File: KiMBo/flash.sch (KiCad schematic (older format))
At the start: 31 parts, among them IC1 24LC32AT-I/OT, U2 OSD3358, U6 74LVC1G06, U7 EMMC**G-S100

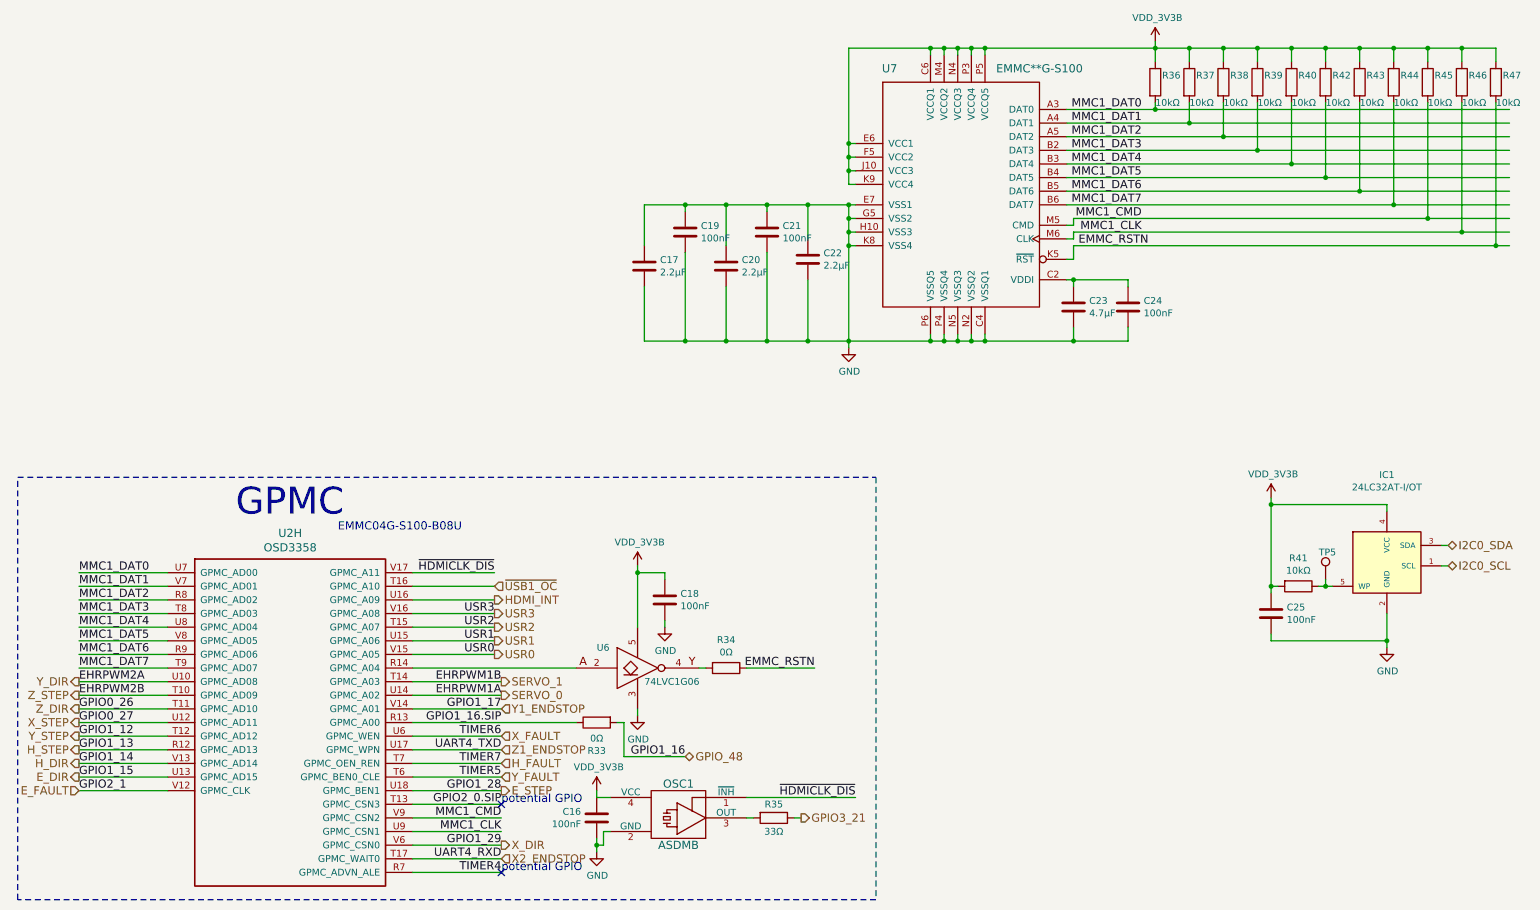
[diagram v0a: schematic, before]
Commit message: Add equivalent annotations document, associate more footprints
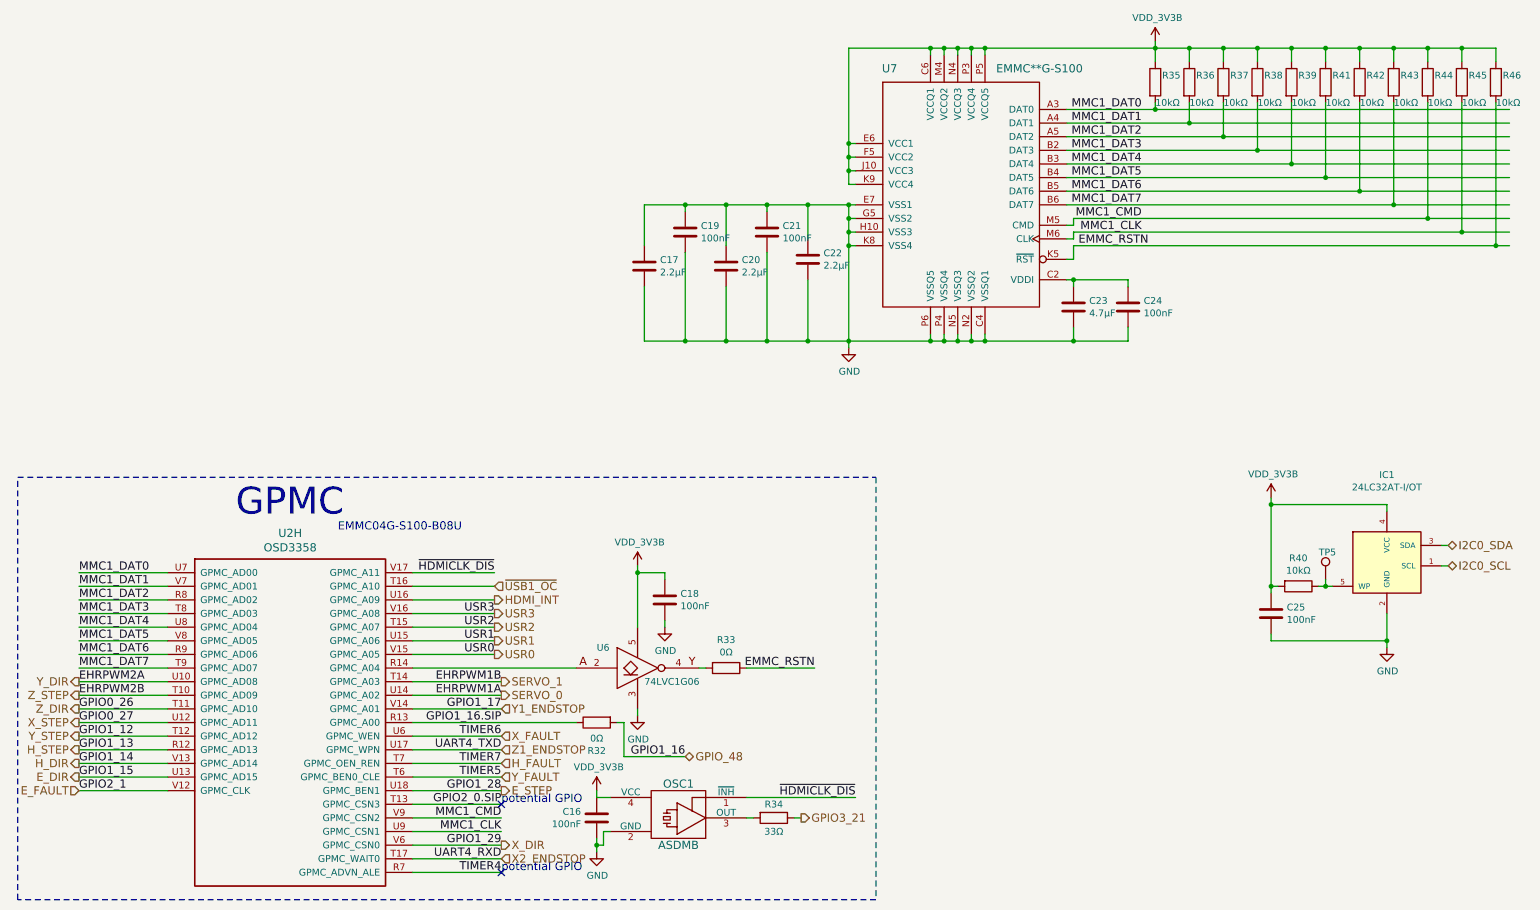
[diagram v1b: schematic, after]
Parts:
- C16, C18, C19, C21, C24, C25: footprint (none) -> Capacitors_SMD:C_0402
- C17, C20, C22, C23: footprint (none) -> Capacitors_SMD:C_0805
- R32: renamed from R33; footprint (none) -> Resistors_SMD:R_0402
- R33: renamed from R34; footprint (none) -> Resistors_SMD:R_0402
- R35: renamed from R36; footprint (none) -> Resistors_SMD:R_0402
- R36: renamed from R37; footprint (none) -> Resistors_SMD:R_0402
- R37: renamed from R38; footprint (none) -> Resistors_SMD:R_0402
- R38: renamed from R39; footprint (none) -> Resistors_SMD:R_0402
- R39: renamed from R40; footprint (none) -> Resistors_SMD:R_0402
- R40: renamed from R41; footprint (none) -> Resistors_SMD:R_0402
- R41: renamed from R42; footprint (none) -> Resistors_SMD:R_0402
- R42: renamed from R43; footprint (none) -> Resistors_SMD:R_0402
- R43: renamed from R44; footprint (none) -> Resistors_SMD:R_0402
- R44: renamed from R45; footprint (none) -> Resistors_SMD:R_0402
- R45: renamed from R46; footprint (none) -> Resistors_SMD:R_0402
- R46: renamed from R47; footprint (none) -> Resistors_SMD:R_0402
- renumbered R35 to R34
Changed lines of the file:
@@
 $EndDescr
 $Comp
-L R R36
+L R R35
 U 1 1 58938DE0
 P 10550 2900
-F 0 "R36" H 10600 2950 50  0000 L CNN
+F 0 "R35" H 10600 2950 50  0000 L CNN
 F 1 "10kΩ" H 10550 2750 50  0000 L CNN
-F 2 "" V 10480 2900 50  0001 C CNN
+F 2 "Resistors_SMD:R_0402" V 10480 2900 50  0001 C CNN
 F 3 "" H 10550 2900 50  0000 C CNN
 	1    10550 2900
@@
 $EndComp
 $Comp
-L R R37
+L R R36
 U 1 1 58938E26
 P 10800 2900
-F 0 "R37" H 10850 2950 50  0000 L CNN
+F 0 "R36" H 10850 2950 50  0000 L CNN
 F 1 "10kΩ" H 10800 2750 50  0000 L CNN
-F 2 "" V 10730 2900 50  0001 C CNN
+F 2 "Resistors_SMD:R_0402" V 10730 2900 50  0001 C CNN
 F 3 "" H 10800 2900 50  0000 C CNN
 	1    10800 2900
@@
 $EndComp
 $Comp
-L R R38
+L R R37
 U 1 1 58938E51
 P 11050 2900
-F 0 "R38" H 11100 2950 50  0000 L CNN
+F 0 "R37" H 11100 2950 50  0000 L CNN
 F 1 "10kΩ" H 11050 2750 50  0000 L CNN
-F 2 "" V 10980 2900 50  0001 C CNN
+F 2 "Resistors_SMD:R_0402" V 10980 2900 50  0001 C CNN
 F 3 "" H 11050 2900 50  0000 C CNN
 	1    11050 2900
@@
 $EndComp
 $Comp
-L R R39
+L R R38
 U 1 1 58938E75
 P 11300 2900
-F 0 "R39" H 11350 2950 50  0000 L CNN
+F 0 "R38" H 11350 2950 50  0000 L CNN
 F 1 "10kΩ" H 11300 2750 50  0000 L CNN
-F 2 "" V 11230 2900 50  0001 C CNN
+F 2 "Resistors_SMD:R_0402" V 11230 2900 50  0001 C CNN
 F 3 "" H 11300 2900 50  0000 C CNN
 	1    11300 2900
@@
 $EndComp
 $Comp
-L R R40
+L R R39
 U 1 1 58938EA0
 P 11550 2900
-F 0 "R40" H 11600 2950 50  0000 L CNN
+F 0 "R39" H 11600 2950 50  0000 L CNN
 F 1 "10kΩ" H 11550 2750 50  0000 L CNN
-F 2 "" V 11480 2900 50  0001 C CNN
+F 2 "Resistors_SMD:R_0402" V 11480 2900 50  0001 C CNN
 F 3 "" H 11550 2900 50  0000 C CNN
 	1    11550 2900
@@
 $EndComp
 $Comp
-L R R42
+L R R41
 U 1 1 58938F20
 P 11800 2900
-F 0 "R42" H 11850 2950 50  0000 L CNN
+F 0 "R41" H 11850 2950 50  0000 L CNN
 F 1 "10kΩ" H 11800 2750 50  0000 L CNN
-F 2 "" V 11730 2900 50  0001 C CNN
+F 2 "Resistors_SMD:R_0402" V 11730 2900 50  0001 C CNN
 F 3 "" H 11800 2900 50  0000 C CNN
 	1    11800 2900
@@
 	9300 4800 9300 4750
 $Comp
-L R R43
+L R R42
 U 1 1 5893A6C3
 P 12050 2900
-F 0 "R43" H 12100 2950 50  0000 L CNN
+F 0 "R42" H 12100 2950 50  0000 L CNN
 F 1 "10kΩ" H 12050 2750 50  0000 L CNN
-F 2 "" V 11980 2900 50  0001 C CNN
+F 2 "Resistors_SMD:R_0402" V 11980 2900 50  0001 C CNN
 F 3 "" H 12050 2900 50  0000 C CNN
 	1    12050 2900
@@
 $EndComp
 $Comp
-L R R44
+L R R43
 U 1 1 5893A6FB
 P 12300 2900
-F 0 "R44" H 12350 2950 50  0000 L CNN
+F 0 "R43" H 12350 2950 50  0000 L CNN
 F 1 "10kΩ" H 12300 2750 50  0000 L CNN
-F 2 "" V 12230 2900 50  0001 C CNN
+F 2 "Resistors_SMD:R_0402" V 12230 2900 50  0001 C CNN
 F 3 "" H 12300 2900 50  0000 C CNN
 	1    12300 2900
@@
 $EndComp
 $Comp
-L R R45
+L R R44
 U 1 1 5893A736
 P 12550 2900
-F 0 "R45" H 12600 2950 50  0000 L CNN
+F 0 "R44" H 12600 2950 50  0000 L CNN
 F 1 "10kΩ" H 12550 2750 50  0000 L CNN
-F 2 "" V 12480 2900 50  0001 C CNN
+F 2 "Resistors_SMD:R_0402" V 12480 2900 50  0001 C CNN
 F 3 "" H 12550 2900 50  0000 C CNN
 	1    12550 2900
@@
 	10550 3100 10550 3050
 $Comp
-L R R46
+L R R45
 U 1 1 5893AC56
 P 12800 2900
-F 0 "R46" H 12850 2950 50  0000 L CNN
+F 0 "R45" H 12850 2950 50  0000 L CNN
 F 1 "10kΩ" H 12800 2750 50  0000 L CNN
-F 2 "" V 12730 2900 50  0001 C CNN
+F 2 "Resistors_SMD:R_0402" V 12730 2900 50  0001 C CNN
 F 3 "" H 12800 2900 50  0000 C CNN
 	1    12800 2900
@@
 $EndComp
 $Comp
-L R R47
+L R R46
 U 1 1 5893AC8F
 P 13050 2900
-F 0 "R47" H 13100 2950 50  0000 L CNN
+F 0 "R46" H 13100 2950 50  0000 L CNN
 F 1 "10kΩ" H 13050 2750 50  0000 L CNN
-F 2 "" V 12980 2900 50  0001 C CNN
+F 2 "Resistors_SMD:R_0402" V 12980 2900 50  0001 C CNN
 F 3 "" H 13050 2900 50  0000 C CNN
 	1    13050 2900
@@
 Connection ~ 12800 2650
 $Comp
-L GND #PWR099
+L GND #PWR098
 U 1 1 5893C2D6
 P 8300 4850
-F 0 "#PWR099" H 8300 4600 50  0001 C CNN
+F 0 "#PWR098" H 8300 4600 50  0001 C CNN
 F 1 "GND" H 8305 4677 50  0000 C CNN
 F 2 "" H 8300 4850 50  0000 C CNN
@@
 F 0 "C23" H 10065 4596 50  0000 L CNN
 F 1 "4.7μF" H 10065 4505 50  0000 L CNN
-F 2 "" H 9950 4550 50  0001 C CNN
+F 2 "Capacitors_SMD:C_0805" H 9950 4550 50  0001 C CNN
 F 3 "" H 9950 4550 50  0000 C CNN
 	1    9950 4550
@@
 F 0 "C24" H 10465 4596 50  0000 L CNN
 F 1 "100nF" H 10465 4505 50  0000 L CNN
-F 2 "" H 10350 4550 50  0001 C CNN
+F 2 "Capacitors_SMD:C_0402" H 10350 4550 50  0001 C CNN
 F 3 "" H 10350 4550 50  0000 C CNN
 	1    10350 4550
@@
 F 0 "C22" H 8115 4246 50  0000 L CNN
 F 1 "2.2μF" H 8115 4155 50  0000 L CNN
-F 2 "" H 8000 4200 50  0001 C CNN
+F 2 "Capacitors_SMD:C_0805" H 8000 4200 50  0001 C CNN
 F 3 "" H 8000 4200 50  0000 C CNN
 	1    8000 4200
@@
 F 0 "C21" H 7815 4046 50  0000 L CNN
 F 1 "100nF" H 7815 3955 50  0000 L CNN
-F 2 "" H 7700 4000 50  0001 C CNN
+F 2 "Capacitors_SMD:C_0402" H 7700 4000 50  0001 C CNN
 F 3 "" H 7700 4000 50  0000 C CNN
 	1    7700 4000
@@
 F 0 "C20" H 7515 4296 50  0000 L CNN
 F 1 "2.2μF" H 7515 4205 50  0000 L CNN
-F 2 "" H 7400 4250 50  0001 C CNN
+F 2 "Capacitors_SMD:C_0805" H 7400 4250 50  0001 C CNN
 F 3 "" H 7400 4250 50  0000 C CNN
 	1    7400 4250
@@
 F 0 "C19" H 7215 4046 50  0000 L CNN
 F 1 "100nF" H 7215 3955 50  0000 L CNN
-F 2 "" H 7100 4000 50  0001 C CNN
+F 2 "Capacitors_SMD:C_0402" H 7100 4000 50  0001 C CNN
 F 3 "" H 7100 4000 50  0000 C CNN
 	1    7100 4000
@@
 F 0 "C17" H 6915 4296 50  0000 L CNN
 F 1 "2.2μF" H 6915 4205 50  0000 L CNN
-F 2 "" H 6800 4250 50  0001 C CNN
+F 2 "Capacitors_SMD:C_0805" H 6800 4250 50  0001 C CNN
 F 3 "" H 6800 4250 50  0000 C CNN
 	1    6800 4250
@@
 $EndComp
 $Comp
-L R R41
+L R R40
 U 1 1 589CA43D
 P 11600 6600
-F 0 "R41" V 11393 6600 50  0000 C CNN
+F 0 "R40" V 11393 6600 50  0000 C CNN
 F 1 "10kΩ" V 11484 6600 50  0000 C CNN
-F 2 "" V 11530 6600 50  0001 C CNN
+F 2 "Resistors_SMD:R_0402" V 11530 6600 50  0001 C CNN
 F 3 "" H 11600 6600 50  0000 C CNN
 	1    11600 6600
@@
 F 0 "C25" H 11515 6846 50  0000 L CNN
 F 1 "100nF" H 11515 6755 50  0000 L CNN
-F 2 "" H 11400 6800 50  0001 C CNN
+F 2 "Capacitors_SMD:C_0402" H 11400 6800 50  0001 C CNN
 F 3 "" H 11400 6800 50  0000 C CNN
 	1    11400 6800
@@
 	11400 7000 11400 6950
 $Comp
-L GND #PWR0100
+L GND #PWR099
 U 1 1 589CAA98
 P 12250 7050
-F 0 "#PWR0100" H 12250 6800 50  0001 C CNN
+F 0 "#PWR099" H 12250 6800 50  0001 C CNN
 F 1 "GND" H 12255 6877 50  0000 C CNN
 F 2 "" H 12250 7050 50  0000 C CNN
@@
 GPIO1_16.SIP
 $Comp
-L R R33
+L R R32
 U 1 1 58ED6392
 P 6450 7600
-F 0 "R33" V 6657 7600 50  0000 C CNN
+F 0 "R32" V 6657 7600 50  0000 C CNN
 F 1 "0Ω" V 6566 7600 50  0000 C CNN
-F 2 "" V 6380 7600 50  0001 C CNN
+F 2 "Resistors_SMD:R_0402" V 6380 7600 50  0001 C CNN
 F 3 "" H 6450 7600 50  0000 C CNN
 	1    6450 7600
@@
 $EndComp
 $Comp
-L GND #PWR0101
+L GND #PWR0100
 U 1 1 58ED63A5
 P 6750 7550
-F 0 "#PWR0101" H 6750 7300 50  0001 C CNN
+F 0 "#PWR0100" H 6750 7300 50  0001 C CNN
 F 1 "GND" H 6755 7377 50  0000 C CNN
 F 2 "" H 6750 7550 50  0000 C CNN
@@
 F 0 "C18" H 7065 6746 50  0000 L CNN
 F 1 "100nF" H 7065 6655 50  0000 L CNN
-F 2 "" H 6988 6550 50  0001 C CNN
+F 2 "Capacitors_SMD:C_0402" H 6988 6550 50  0001 C CNN
 F 3 "" H 6950 6700 50  0000 C CNN
 	1    6950 6700
@@
 $EndComp
 $Comp
-L GND #PWR0102
+L GND #PWR0101
 U 1 1 58ED63B8
 P 6950 6900
-F 0 "#PWR0102" H 6950 6650 50  0001 C CNN
+F 0 "#PWR0101" H 6950 6650 50  0001 C CNN
 F 1 "GND" H 6955 6727 50  0000 C CNN
 F 2 "" H 6950 6900 50  0000 C CNN
@@
 $EndComp
 $Comp
-L R R34
+L R R33
 U 1 1 58ED63BE
 P 7400 7200
-F 0 "R34" V 7193 7200 50  0000 C CNN
+F 0 "R33" V 7193 7200 50  0000 C CNN
 F 1 "0Ω" V 7284 7200 50  0000 C CNN
-F 2 "" V 7330 7200 50  0001 C CNN
+F 2 "Resistors_SMD:R_0402" V 7330 7200 50  0001 C CNN
 F 3 "" H 7400 7200 50  0000 C CNN
 	1    7400 7200
@@
 F 0 "C16" H 6565 8346 50  0000 L CNN
 F 1 "100nF" H 6565 8255 50  0000 L CNN
-F 2 "" H 6450 8300 50  0001 C CNN
+F 2 "Capacitors_SMD:C_0402" H 6450 8300 50  0001 C CNN
 F 3 "" H 6450 8300 50  0000 C CNN
 	1    6450 8300
@@
 $EndComp
 $Comp
-L GND #PWR0103
+L GND #PWR0102
 U 1 1 58ED63D4
 P 6450 8550
-F 0 "#PWR0103" H 6450 8300 50  0001 C CNN
+F 0 "#PWR0102" H 6450 8300 50  0001 C CNN
 F 1 "GND" H 6455 8377 50  0000 C CNN
 F 2 "" H 6450 8550 50  0000 C CNN
@@
 $EndComp
 $Comp
-L R R35
+L R R34
 U 1 1 58ED63E0
 P 7750 8300
-F 0 "R35" V 7650 8300 50  0000 C CNN
+F 0 "R34" V 7650 8300 50  0000 C CNN
 F 1 "33Ω" V 7850 8300 50  0000 C CNN
 F 2 "" V 7680 8300 50  0001 C CNN
@@
 SERVO_0
 $Comp
-L VDD_3V3B #PWR0104
+L VDD_3V3B #PWR0103
 U 1 1 59E9BAE0
 P 10550 2600
-F 0 "#PWR0104" H 10550 2450 50  0001 C CNN
+F 0 "#PWR0103" H 10550 2450 50  0001 C CNN
 F 1 "VDD_3V3B" H 10565 2773 50  0000 C CNN
 F 2 "" H 10550 2600 50  0000 C CNN
@@
 USR0
 $Comp
-L VDD_3V3B #PWR0105
+L VDD_3V3B #PWR0104
 U 1 1 59FAFB00
 P 6450 8100
-F 0 "#PWR0105" H 6450 7950 50  0001 C CNN
+F 0 "#PWR0104" H 6450 7950 50  0001 C CNN
 F 1 "VDD_3V3B" H 6465 8273 50  0000 C CNN
 F 2 "" H 6450 8100 50  0000 C CNN
@@
 $EndComp
 $Comp
-L VDD_3V3B #PWR0106
+L VDD_3V3B #PWR0105
 U 1 1 59FBC4DE
 P 6750 6450
-F 0 "#PWR0106" H 6750 6300 50  0001 C CNN
+F 0 "#PWR0105" H 6750 6300 50  0001 C CNN
 F 1 "VDD_3V3B" H 6765 6623 50  0000 C CNN
 F 2 "" H 6750 6450 50  0000 C CNN
@@
 Connection ~ 11400 6600
 $Comp
-L VDD_3V3B #PWR0107
+L VDD_3V3B #PWR0106
 U 1 1 59FBD7EE
 P 11400 5950
-F 0 "#PWR0107" H 11400 5800 50  0001 C CNN
+F 0 "#PWR0106" H 11400 5800 50  0001 C CNN
 F 1 "VDD_3V3B" H 11415 6123 50  0000 C CNN
 F 2 "" H 11400 5950 50  0000 C CNN
